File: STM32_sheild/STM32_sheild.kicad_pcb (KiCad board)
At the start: 2 copper layers, 70 x 57.5 mm, 5 parts, among them J1 CN7, J2 CN10

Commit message: Placing first components on schematic
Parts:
- added J3: 61612002121503, KiCad_SMB_coax:61612002121503, F.Cu at (122.0, 102.5)
- added U1: MCP73831-2-MC, Package_DFN_QFN:DFN-8-1EP_3x2mm_P0.5mm_EP1.7x1.4mm, F.Cu at (126.9, 94.8)
- added U2: OPA333xxDBV, Package_TO_SOT_SMD:SOT-23-5, F.Cu at (114.9, 93.5)
- added U4: TPS63031DSK, Package_SON:WSON-10-1EP_2.5x2.5mm_P0.5mm_EP1.2x2mm, F.Cu at (131.8, 103.5)
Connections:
- J1 pad 28: unconnected-(J1-Pin_28-Pad28) -> /ADC1
- J1 pad 30: unconnected-(J1-Pin_30-Pad30) -> /ADC2

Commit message: more changes to schematic mainly
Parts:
- added B1: 1042P, 18650_cradle:1042P_KEY, F.Cu at (190.0, 77.0)
- added C1: 10uF, Capacitor_SMD:C_0805_2012Metric, F.Cu at (145.1, 90.0)
- added C2: 10uF, Capacitor_SMD:C_0805_2012Metric, F.Cu at (145.1, 93.0)
- added C3: 100n, Capacitor_SMD:C_0805_2012Metric, F.Cu at (145.1, 96.0)
- added C4: 4.7uF, Capacitor_SMD:C_0805_2012Metric, F.Cu at (202.7, 121.0)
- added C5: 4.7uF, Capacitor_SMD:C_0805_2012Metric, F.Cu at (205.7, 121.0)
- added C6: 100n, Capacitor_SMD:C_0805_2012Metric, F.Cu at (208.7, 121.0)
- added C7: 10uF, Capacitor_SMD:C_0805_2012Metric, F.Cu at (211.7, 121.0)
- added C8: 10uF, Capacitor_SMD:C_0805_2012Metric, F.Cu at (214.7, 121.0)
- added C9: 10uF, Capacitor_SMD:C_0805_2012Metric, F.Cu at (217.7, 121.0)
- added D1: ESD9B3.3ST5G, Diode_SMD:D_SOD-923, F.Cu at (126.4, 89.5)
- added J4: 632722100213, KiCad_wurth_USB-C_PD_connector:632722100213, F.Cu at (207.1, 112.0)
- added JP1: Jumper_3_Bridged12, Jumper:SolderJumper-3_P1.3mm_Bridged2Bar12_Pad1.0x1.5mm, F.Cu at (145.7, 99.3)
- added L2: LPS3015-152MRC, LPS3015-152MRC:IND_LPS3015-152MRC, F.Cu at (203.5, 97.9)
- added R1: 10k, Resistor_SMD:R_0805_2012Metric, F.Cu at (140.7, 90.0)
- added R2: 330k, Resistor_SMD:R_0805_2012Metric, F.Cu at (140.7, 92.9)
- added R3: 2.2k, Resistor_SMD:R_0805_2012Metric, F.Cu at (140.7, 95.9)
- added R4: 10R, Resistor_SMD:R_0805_2012Metric, F.Cu at (140.7, 98.8)
- added R5: 100R, Resistor_SMD:R_0805_2012Metric, F.Cu at (140.7, 101.8)
- added R6: 5.1k, Resistor_SMD:R_0805_2012Metric, F.Cu at (202.6, 103.0)
- added R7: 5.1k, Resistor_SMD:R_0805_2012Metric, F.Cu at (205.6, 103.0)
- added R8: 2k, Resistor_SMD:R_0805_2012Metric, F.Cu at (208.5, 103.0)
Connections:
- net Net-(U1-V_{DD}-Pad1) renamed V_USB
- J1 pad 33: +BATT -> unconnected-(J1-Pin_33-Pad33)
- J2 pad 32: GNDA -> GND
- J3 pad 1: unconnected-(J3-Pad1) -> Net-(J3-Pad1)
- J3 pad 2: GNDA -> GND
- J3 pad 3: GNDA -> GND
- J3 pad 4: GNDA -> GND
- J3 pad 5: GNDA -> GND
- U1 pad 3: Net-(U1-V_{BAT}-Pad3) -> +BATT
- U1 pad 4: Net-(U1-V_{BAT}-Pad3) -> +BATT
- U1 pad 5: unconnected-(U1-STAT-Pad5) -> Net-(U1-STAT)
- U1 pad 6: unconnected-(U1-V_{SS}-Pad6) -> GND
- U2 pad 1: unconnected-(U2-Pad1) -> Net-(R2-Pad2)
- U2 pad 2: unconnected-(U2-V--Pad2) -> GND
- U2 pad 3: /ADC1 -> Net-(D1-A1)
- U2 pad 4: unconnected-(U2---Pad4) -> Net-(U2--)
- U2 pad 5: unconnected-(U2-V+-Pad5) -> Net-(U2-V+)
- U4 pad 1: unconnected-(U4-VOUT-Pad1) -> +3.3V
- U4 pad 10: unconnected-(U4-FB-Pad10) -> +3.3V
- U4 pad 11: Net-(U4-PGND-Pad11) -> GND
- U4 pad 2: unconnected-(U4-L2-Pad2) -> Net-(U4-L2)
- U4 pad 3: Net-(U4-PGND-Pad11) -> GND
- U4 pad 4: unconnected-(U4-L1-Pad4) -> Net-(U4-L1)
- U4 pad 5: unconnected-(U4-VIN-Pad5) -> +BATT
- U4 pad 6: unconnected-(U4-EN-Pad6) -> Net-(U4-EN)
- U4 pad 7: unconnected-(U4-PS/SYNC-Pad7) -> Net-(U4-EN)
- U4 pad 8: unconnected-(U4-VINA-Pad8) -> Net-(U4-EN)
- U4 pad 9: unconnected-(U4-GND-Pad9) -> GND

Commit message: more changes to schematic and layout
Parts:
- added D2: LED, LED_SMD:LED_0805_2012Metric, F.Cu at (147.2, 82.0)
- added D3: LED, LED_SMD:LED_0805_2012Metric, F.Cu at (155.7, 101.3)
- added J5: 691210910002, KiCad_wurth_2-pin_screw_terminal:691210910002, F.Cu at (156.5, 95.0)
- added R10: 470R, Resistor_SMD:R_0805_2012Metric, F.Cu at (160.1, 101.3)
- added R9: 470R, Resistor_SMD:R_0805_2012Metric, F.Cu at (136.2, 81.0)
- moved J4 4.45 mm to (211.5, 112.0)
- renumbered L2 to L1
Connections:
- net Net-(D1-A1) renamed /OPA_IN+
- net Net-(R2-Pad2) renamed /OPA_out
- net Net-(U2--) renamed /OPA_IN-
- net Net-(U2-V+) renamed /OPA_VDD
- C8 pad 1: +3.3V -> +3.3V_REG
- C9 pad 1: +3.3V -> +3.3V_REG
- J2 pad 7: unconnected-(J2-Pin_7-Pad7) -> VDDA
- J2 pad 9: unconnected-(J2-Pin_9-Pad9) -> GND
- JP1 pad 1: unconnected-(JP1-A-Pad1) -> VDD
- JP1 pad 2: unconnected-(JP1-C-Pad2) -> Net-(JP1-C)
- JP1 pad 3: unconnected-(JP1-B-Pad3) -> +3.3V
- L1 pad 1: unconnected-(L2-Pad1) -> Net-(U4-L2)
- L1 pad 2: unconnected-(L2-Pad2) -> Net-(U4-L1)
- R4 pad 2: VDD -> Net-(JP1-C)
- R8 pad 1: Net-(U1-STAT) -> Net-(U1-PROG)
- U1 pad 8: unconnected-(U1-PROG-Pad8) -> Net-(U1-PROG)
- U4 pad 1: +3.3V -> +3.3V_REG
- U4 pad 10: +3.3V -> +3.3V_REG

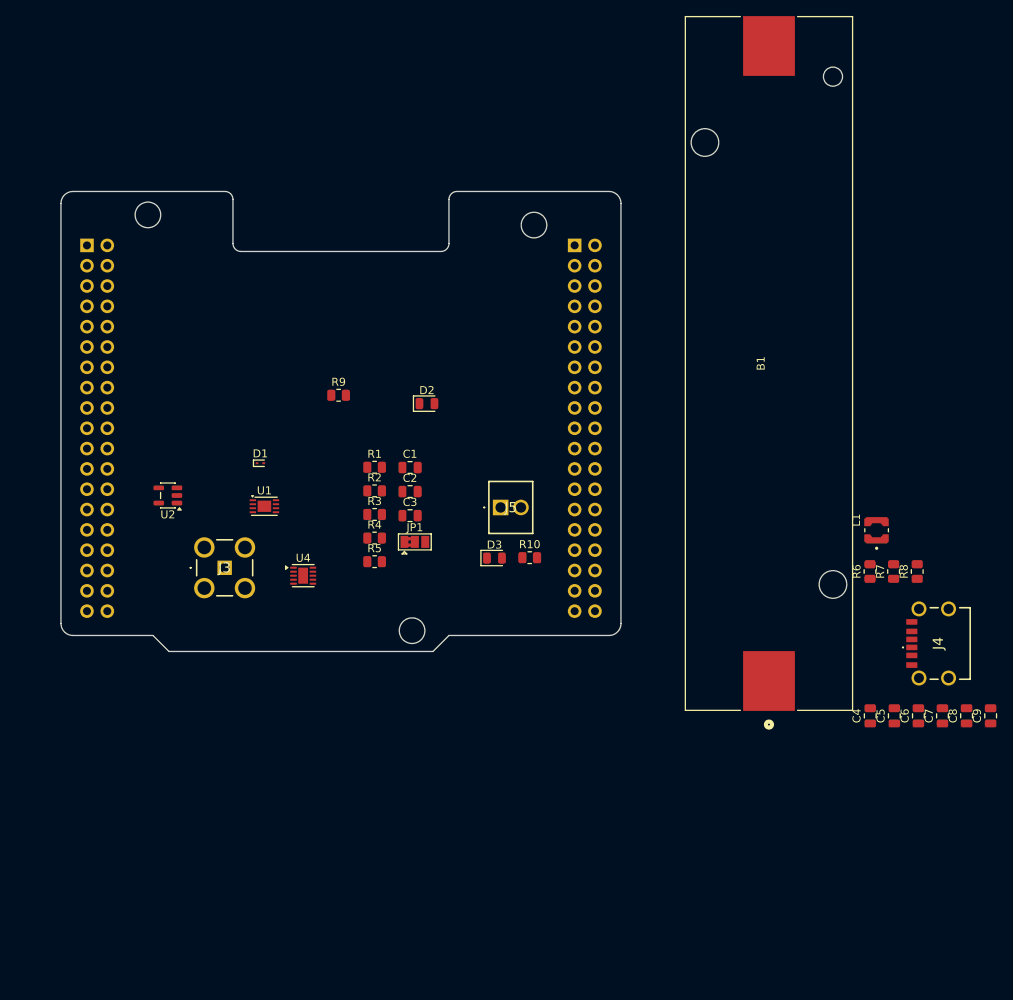
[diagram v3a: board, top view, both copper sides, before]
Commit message: Starting layout routing
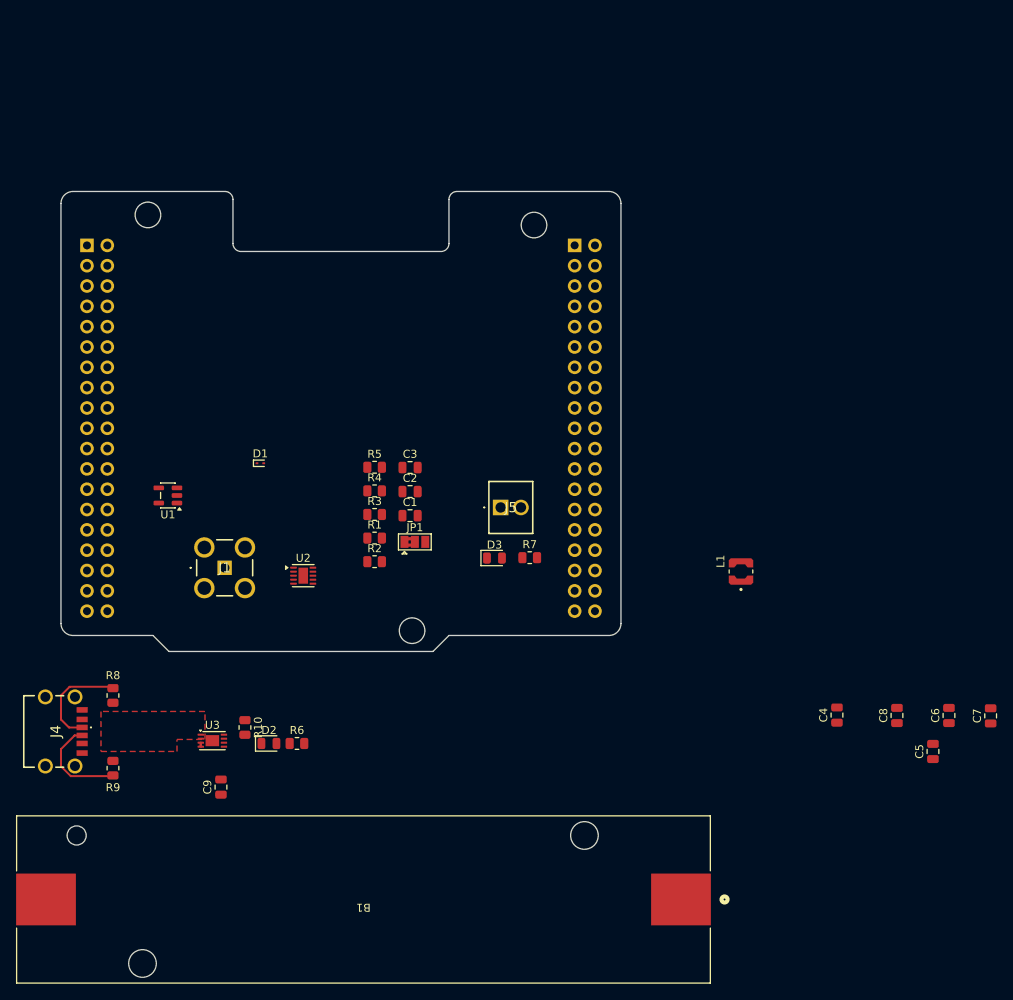
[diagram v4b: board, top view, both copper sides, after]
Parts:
- moved J4 111.5 mm to (100.5, 123.0), turned to -90 degrees
- moved R8 98.8 mm to (108.0, 118.5), turned to -90 degrees
- moved R9 97.8 mm to (108.0, 127.6)
- moved R10 86.3 mm to (124.5, 122.5), turned to -90 degrees
- moved C9 84.6 mm to (121.5, 129.9)
- moved B1 84.0 mm to (139.3, 144.0), turned to 180 degrees
- moved D2 46.8 mm to (127.5, 124.5)
- moved R6 43.8 mm to (131.0, 124.5)
- moved U3 30.0 mm to (120.4, 124.2)
- moved L1 17.7 mm to (186.5, 103.0)
- moved C5 4.61 mm to (210.5, 125.5)
- moved C4 4.16 mm to (198.5, 121.0)
- moved C8 2.68 mm to (206.0, 121.0)
- moved C6 2.20 mm to (212.5, 121.0)
- renumbered C3 to C1, C1 to C3, C7 to C5, C8 to C6, C9 to C7, C6 to C8, C5 to C9, J3 to J1, J1 to J2, J2 to J3, R4 to R1, R8 to R10, R5 to R2, R2 to R4, R1 to R5, R9 to R6, R10 to R7, R7 to R8, R6 to R9, U2 to U1, U4 to U2, U1 to U3
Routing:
- net Net-(J4-CC1): track 0.00 -> 13.1 mm
- net Net-(J4-CC2): track 0.00 -> 12.6 mm
- net +BATT: track 0.00 -> 0.75 mm
- added copper zone on F.Cu, net V_USB

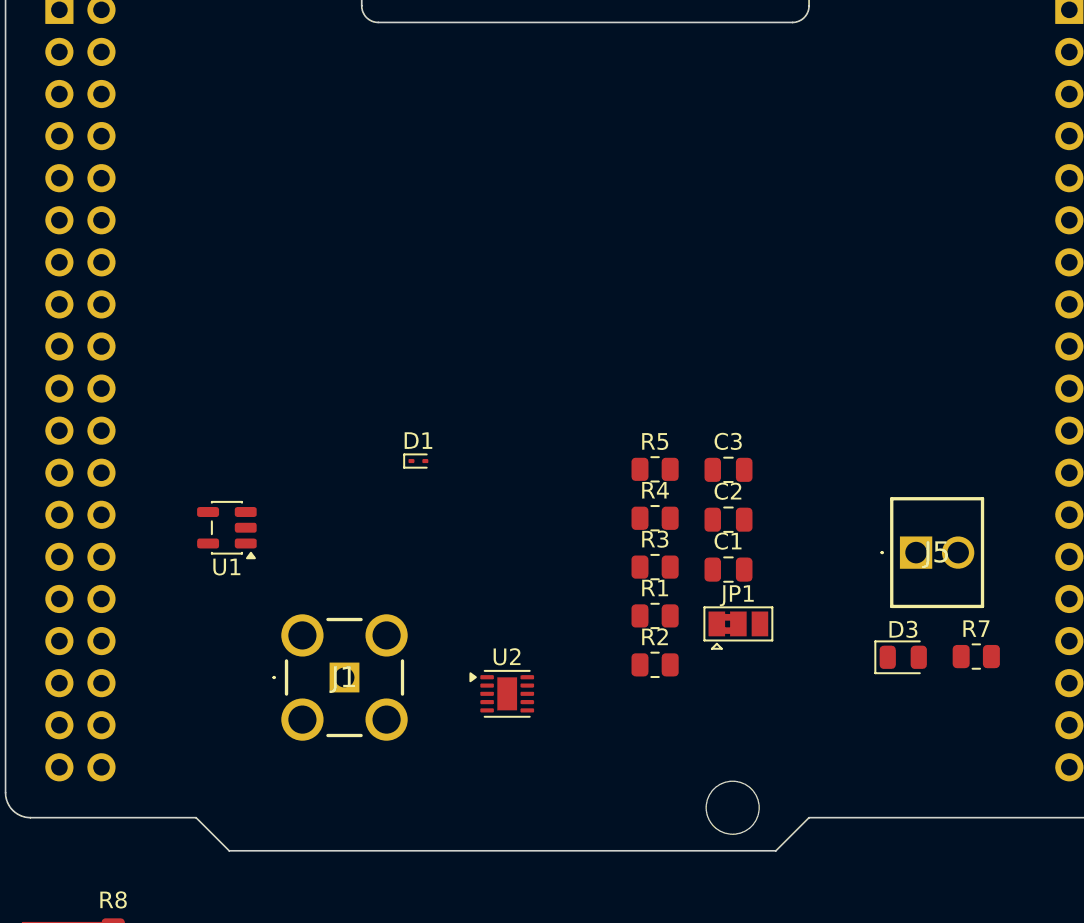
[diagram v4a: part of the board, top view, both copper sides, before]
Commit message: More changes to layout, also added another opamp
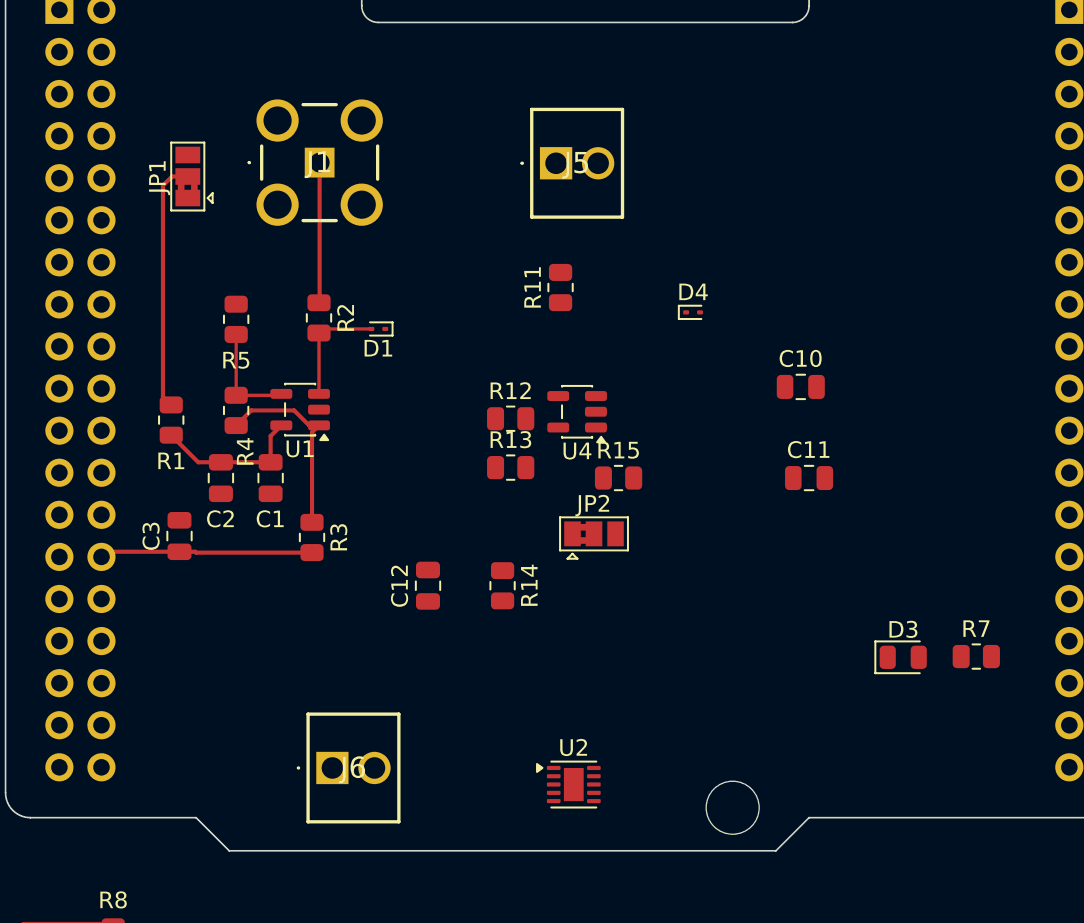
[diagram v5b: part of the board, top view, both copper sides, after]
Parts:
- added C10: 100n, Capacitor_SMD:C_0805_2012Metric, F.Cu at (149.5, 85.0)
- added C11: 10uF, Capacitor_SMD:C_0805_2012Metric, F.Cu at (150.0, 90.5)
- added C12: 10uF, Capacitor_SMD:C_0805_2012Metric, F.Cu at (127.0, 97.0)
- added D4: ESD9B3.3ST5G, Diode_SMD:D_SOD-923, F.Cu at (143.0, 80.5)
- added J6: 691210910002, KiCad_wurth_2-pin_screw_terminal:691210910002, F.Cu at (121.2, 108.0)
- added JP2: Jumper_3_Bridged12, Jumper:SolderJumper-3_P1.3mm_Bridged2Bar12_Pad1.0x1.5mm, F.Cu at (137.0, 93.9)
- added R11: 100R, Resistor_SMD:R_0805_2012Metric, F.Cu at (135.0, 79.0)
- added R12: 10k, Resistor_SMD:R_0805_2012Metric, F.Cu at (132.0, 86.9)
- added R13: 330k, Resistor_SMD:R_0805_2012Metric, F.Cu at (132.0, 89.9)
- added R14: 2.2k, Resistor_SMD:R_0805_2012Metric, F.Cu at (131.5, 97.0)
- added R15: 10R, Resistor_SMD:R_0805_2012Metric, F.Cu at (138.5, 90.5)
- added U4: OPA333xxDBV, Package_TO_SOT_SMD:SOT-23-5, F.Cu at (136.0, 86.5)
- moved JP1 42.8 mm to (112.5, 72.3), turned to 90 degrees
- moved C3 33.4 mm to (112.0, 94.0), turned to 90 degrees
- moved J5 32.0 mm to (134.7, 71.5)
- moved R1 31.5 mm to (111.5, 87.0), turned to 90 degrees
- moved J1 31.1 mm to (120.5, 71.5)
- moved C2 30.7 mm to (114.5, 90.5), turned to -90 degrees
- moved R2 29.2 mm to (120.4, 80.8), turned to -90 degrees
- moved C1 28.2 mm to (117.5, 90.5), turned to -90 degrees
- moved R5 26.9 mm to (115.4, 80.9), turned to 90 degrees
- moved R4 26.1 mm to (115.4, 86.4), turned to -90 degrees
- moved R3 20.8 mm to (120.0, 94.1), turned to -90 degrees
- moved U1 8.39 mm to (119.3, 86.4)
- moved D1 8.33 mm to (124.0, 81.5), turned to 180 degrees
- moved U2 6.79 mm to (135.8, 109.0)
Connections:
- net Net-(J1-Pad1) renamed /Coax_in
- D1 pad 1: /OPA_IN+ -> GND
- D1 pad 2: GND -> /OPA_IN+
- J5 pad 1: unconnected-(J5-Pad1) -> Net-(J5-Pad1)
- J5 pad 2: unconnected-(J5-Pad2) -> GND
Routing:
- net Net-(JP1-C): track 0.00 -> 15.2 mm
- net /ADC1: track 0.00 -> 12.9 mm
- net /OPA_out: track 0.00 -> 11.9 mm
- net /OPA_VDD: track 0.00 -> 9.18 mm
- net /Coax_in: track 0.00 -> 8.48 mm
- net /OPA_IN+: track 0.00 -> 6.94 mm
- net /OPA_IN-: track 0.00 -> 6.44 mm
